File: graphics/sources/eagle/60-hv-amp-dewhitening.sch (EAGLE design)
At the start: 5 parts

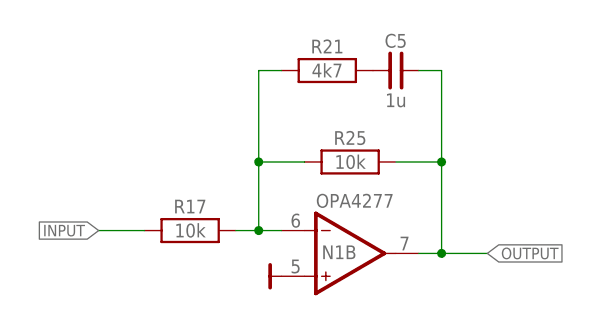
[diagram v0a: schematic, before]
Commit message: Fixed some Eagle graphics and added top and bottom board views to Chapter 6
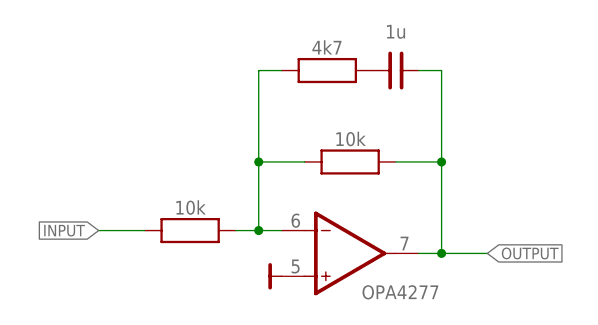
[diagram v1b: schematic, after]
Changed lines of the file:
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@@
 <setting verticaltext="up"/>
 </settings>
-<grid distance="0.1" unitdist="inch" unit="inch" style="lines" multiple="1" display="yes" altdistance="0.025" altunitdist="inch" altunit="inch"/>
+<grid distance="0.1" unitdist="inch" unit="inch" style="lines" multiple="1" display="no" altdistance="0.025" altunitdist="inch" altunit="inch"/>
 <layers>
 <layer number="91" name="Nets" color="34" fill="1" visible="yes" active="yes"/>
@@
 </plain>
 <instances>
-<instance part="R17" gate="A" x="162.56" y="355.6"/>
-<instance part="R25" gate="A" x="180.34" y="363.22"/>
-<instance part="C5" gate="A" x="185.42" y="373.38"/>
+<instance part="R17" gate="A" x="162.56" y="355.6" smashed="yes">
+<attribute name="VALUE" x="162.56" y="358.14" size="1.524" layer="96" font="vector" align="center"/>
+</instance>
+<instance part="R25" gate="A" x="180.34" y="363.22" smashed="yes">
+<attribute name="VALUE" x="180.34" y="365.76" size="1.524" layer="96" font="vector" align="center"/>
+</instance>
+<instance part="C5" gate="A" x="185.42" y="373.38" smashed="yes">
+<attribute name="VALUE" x="185.42" y="378.46" size="1.524" layer="96" font="vector" align="top-center"/>
+</instance>
 <instance part="$6" gate="A" x="172.72" y="350.52" rot="R270"/>
-<instance part="N1" gate="B" x="180.34" y="353.06"/>
-<instance part="R21" gate="A" x="177.8" y="373.38"/>
+<instance part="N1" gate="B" x="180.34" y="353.06" smashed="yes">
+<attribute name="VALUE" x="181.61" y="347.98" size="1.524" layer="96" font="vector"/>
+</instance>
+<instance part="R21" gate="A" x="177.8" y="373.38" smashed="yes">
+<attribute name="VALUE" x="177.8" y="375.92" size="1.524" layer="96" font="vector" align="center"/>
+</instance>
 </instances>
 <busses>
